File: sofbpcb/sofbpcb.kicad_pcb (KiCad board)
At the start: 2 copper layers, 39 x 119 mm, 17 parts, among them J1 MAX98357A_hdr, J2 MPU6050_hdr, J3 5v Power In, J4 LEDStalk_hdr, J5 VibrationMotor_hdr, J6 Teensy4.1_left_hdr, J7 Teensy4.1_right_hdr, U2 ULN2003

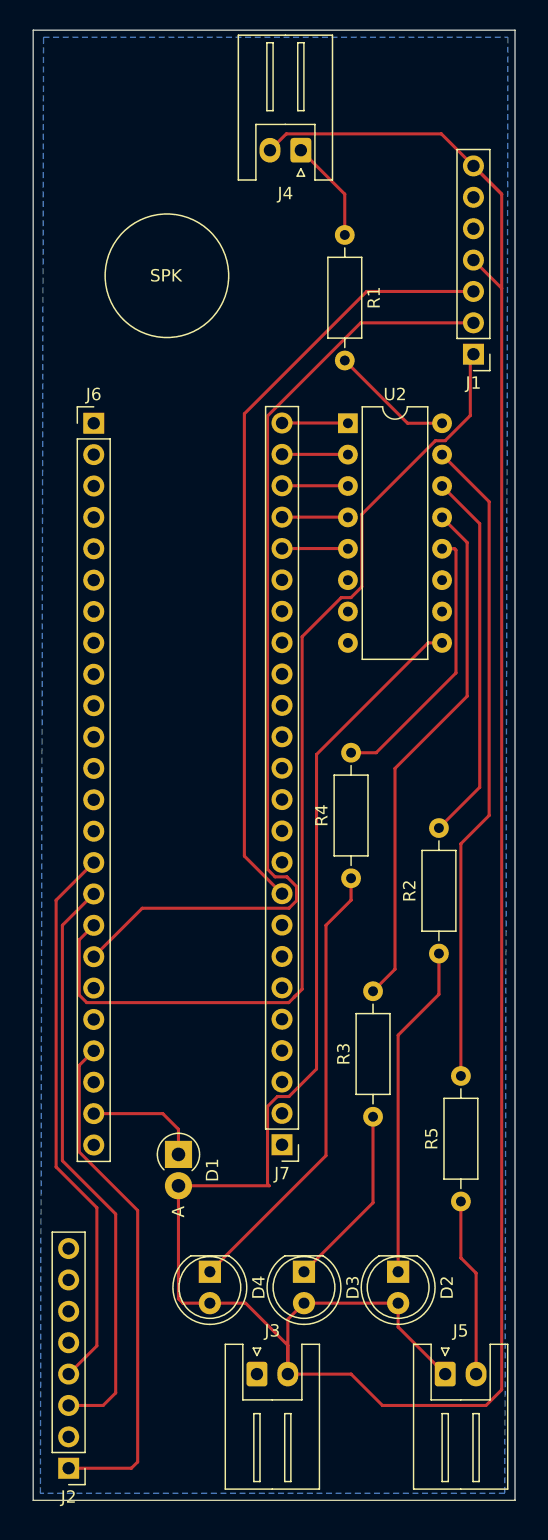
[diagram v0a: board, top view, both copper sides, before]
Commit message: PCB design complete, just needs silk screen tidied up
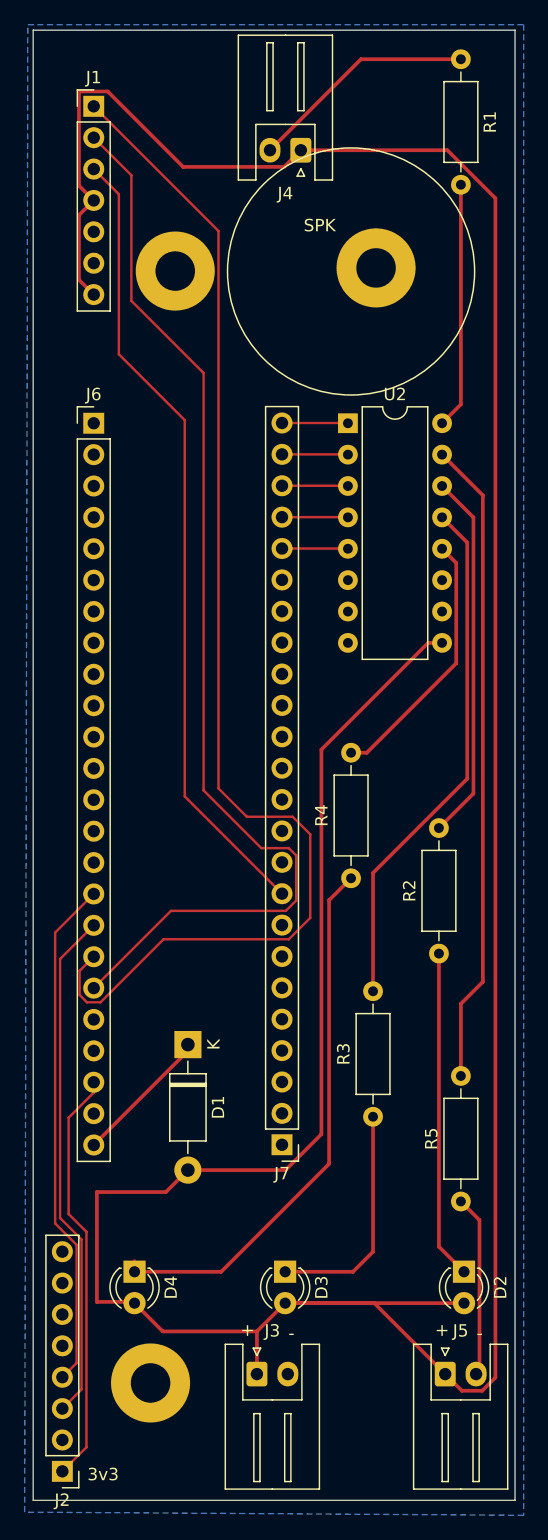
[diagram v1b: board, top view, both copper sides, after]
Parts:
- added REF**: MountingHole_3.2mm_M3_Pad, MountingHole:MountingHole_3.2mm_M3_Pad, F.Cu at (127.8, 55.2)
- added REF**: MountingHole_3.2mm_M3_Pad, MountingHole:MountingHole_3.2mm_M3_Pad, F.Cu at (111.5, 55.5)
- added REF**: MountingHole_3.2mm_M3_Pad, MountingHole:MountingHole_3.2mm_M3_Pad, F.Cu at (109.5, 145.5)
- D1: footprint Diode_THT:D_DO-41_SOD81_P2.54mm_Vertical_AnodeUp -> Diode_THT:D_DO-41_SOD81_P10.16mm_Horizontal
- D2, D3, D4: footprint LED_THT:LED_D5.0mm -> LED_THT:LED_D3.0mm
- moved J1 36.7 mm to (104.9, 42.2), turned to 0 degrees
- moved R1 17.0 mm to (134.6, 38.4)
- moved D1 8.92 mm to (112.5, 118.1)
- moved D4 6.10 mm to (108.2, 136.5)
- moved D2 5.33 mm to (134.9, 136.5)
- moved D3 1.52 mm to (120.4, 136.5)
- moved J2 0.57 mm to (102.4, 152.7)
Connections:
- J3 pad 1: GND -> +5V
- J3 pad 2: +5V -> GND
- J4 pad 1: Net-(J4-Pad1) -> +5V
- J4 pad 2: +5V -> Net-(J4-Pad2)
- J6 pad 15: /SDA -> Net-(J6-Pad15)
- J6 pad 16: /SCL -> /SDA
- J6 pad 17: /LRCLK -> /SCL
- J6 pad 18: /BCLK -> /LRCLK
- J6 pad 19: Net-(J6-Pad19) -> /BCLK
- J6 pad 21: /3v3 -> Net-(J6-Pad21)
- J6 pad 22: GND -> /3v3
- J6 pad 23: /VIN -> GND
- J6 pad 24: Net-(J6-Pad24) -> /VIN
- R1 pad 1: Net-(J4-Pad1) -> Net-(J4-Pad2)
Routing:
- net +5V: track 245.0 -> 281.0 mm
- net Net-(J4-Pad2): track 0.00 -> 18.5 mm
- net /LRCLK: track 83.4 -> 100.4 mm
- net /BCLK: track 78.8 -> 89.2 mm
- net Net-(R1-Pad2): track 9.98 -> 19.9 mm
- net Net-(J4-Pad1): track 8.33 -> 0.00 mm
- net /3v3: track 41.5 -> 33.7 mm
- net Net-(D4-Pad1): track 36.6 -> 44.1 mm
- net /SCL: track 48.2 -> 41.6 mm
- net Net-(D3-Pad1): track 14.9 -> 18.7 mm
- net /SDA: track 45.0 -> 42.4 mm
- net /DigAud: track 62.7 -> 65.0 mm
- net /VIN: track 9.42 -> 11.3 mm
- net Net-(R4-Pad2): track 22.3 -> 21.3 mm
- net Net-(D2-Pad1): track 27.1 -> 26.6 mm
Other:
- net class 5VPWR added: clearance 0.2, trace_width 0.3, via_dia 0.8, via_drill 0.4
- net class Default: trace_width 0.25 -> 0.2
- board text added: "+"
- board text added: "-"
- board text added: "3v3"

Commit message: Added silk screen, plotted gerbers for pcb fab
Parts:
- added G***: LOGO, scepterpcblogo:scepterpcblogo, B.Cu at (118.4, 94.7)
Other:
- board text added: "15"
- board text added: "5v Input"
- board text added: "68"
- board text added: "LEDArray"
- board text added: "LRC"
- board text added: "MPU - SD UP ->"
- board text added: "Phil McCarthy 2021"
- board text added: "Rev v01"
- board text added: "ScepterPCB"
- board text added: "ULN2003"
- board text added: "VibMtr"
